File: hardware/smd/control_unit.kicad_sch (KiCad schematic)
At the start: 29 parts, among them J3 UART, K1 SPDT, 5V 72R, 10A 250VAC, Q1 NPN, 40V, 500mA, SW1 SW_Push, SW2 SW_Push, U5 ESP32-H2, Y1 32MHz ±10ppm CL8pF

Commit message: Add capacitor specifications, change capacity around crystal
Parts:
- C19: renamed from C24; value 10p 10V -> 8p 10V C0G
- C20: renamed from C25; value 10p 10V -> 8p 10V C0G
- renumbered C19 to C21, C20 to C22, C21 to C23, C22 to C24, C23 to C25, D5 to D4, D4 to D5, R9 to R10, R6 to R5, R5 to R6, R10 to R7, R7 to R8, R8 to R9, SW2 to SW1, SW1 to SW2

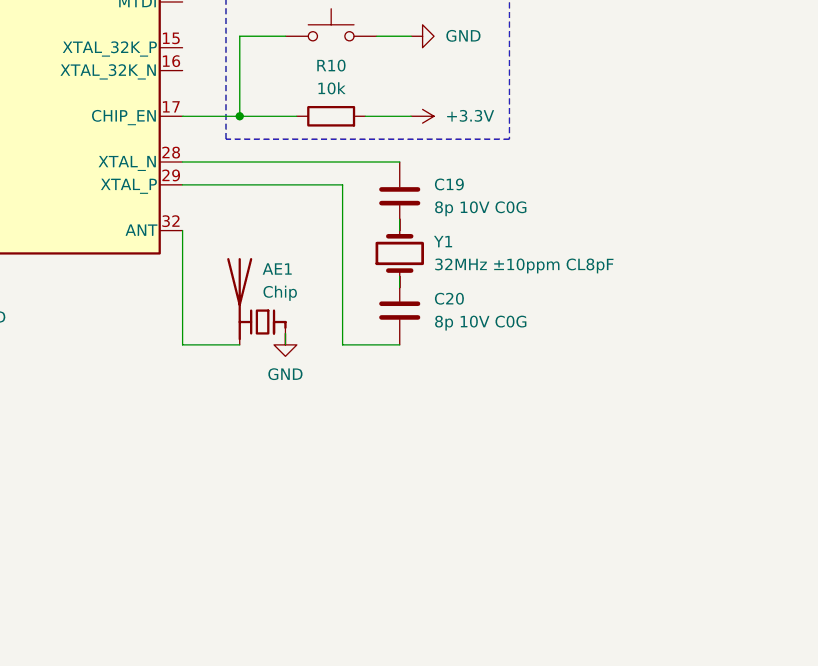
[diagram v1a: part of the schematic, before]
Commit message: Properly layout GND-fed antenna
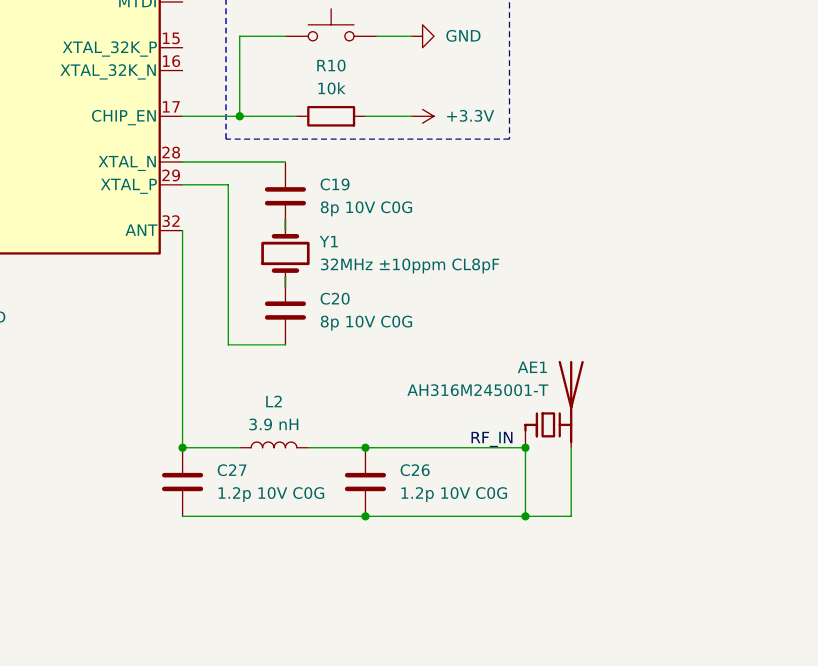
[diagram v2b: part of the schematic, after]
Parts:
- added C26, C27: 1.2p 10V C0G, symbol Device:C
- added L2: 3.9 nH, symbol Device:L
- AE1: value Chip -> AH316M245001-T
- D4: footprint Diode_THT:D_DO-41_SOD81_P10.16mm_Horizontal -> (none)
- D5, D6: footprint LED_THT:LED_D3.0mm -> (none)
- K1: footprint KiCadX_Relays_THT:Relay_SPDT_Relpol-RM51 -> (none)
- Q1: footprint Package_TO_SOT_THT:TO-92_Inline_Wide -> (none)
- R10, R5, R6, R7, R8, R9: footprint Resistor_THT:R_Axial_DIN0207_L6.3mm_D2.5mm_P7.62mm_Horizontal -> (none)
- U5: footprint KiCadX_MCU_Espressif:TQFN_32_1EP_4x4mm_P0.4mm_EP2.6x2.6mm_Standard -> (none)
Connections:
- net GND: no longer AE1.1 (FEED)
- net at U5.32 (ANT): now also C27.2, L2.1; no longer AE1.2 (PCB_Trace)
- new net RF_IN: AE1.1 (FEED), AE1.2 (PCB_Trace), C26.1, C26.2, C27.1, L2.2
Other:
- moved on the sheet: AE1, C19, C20, Y1

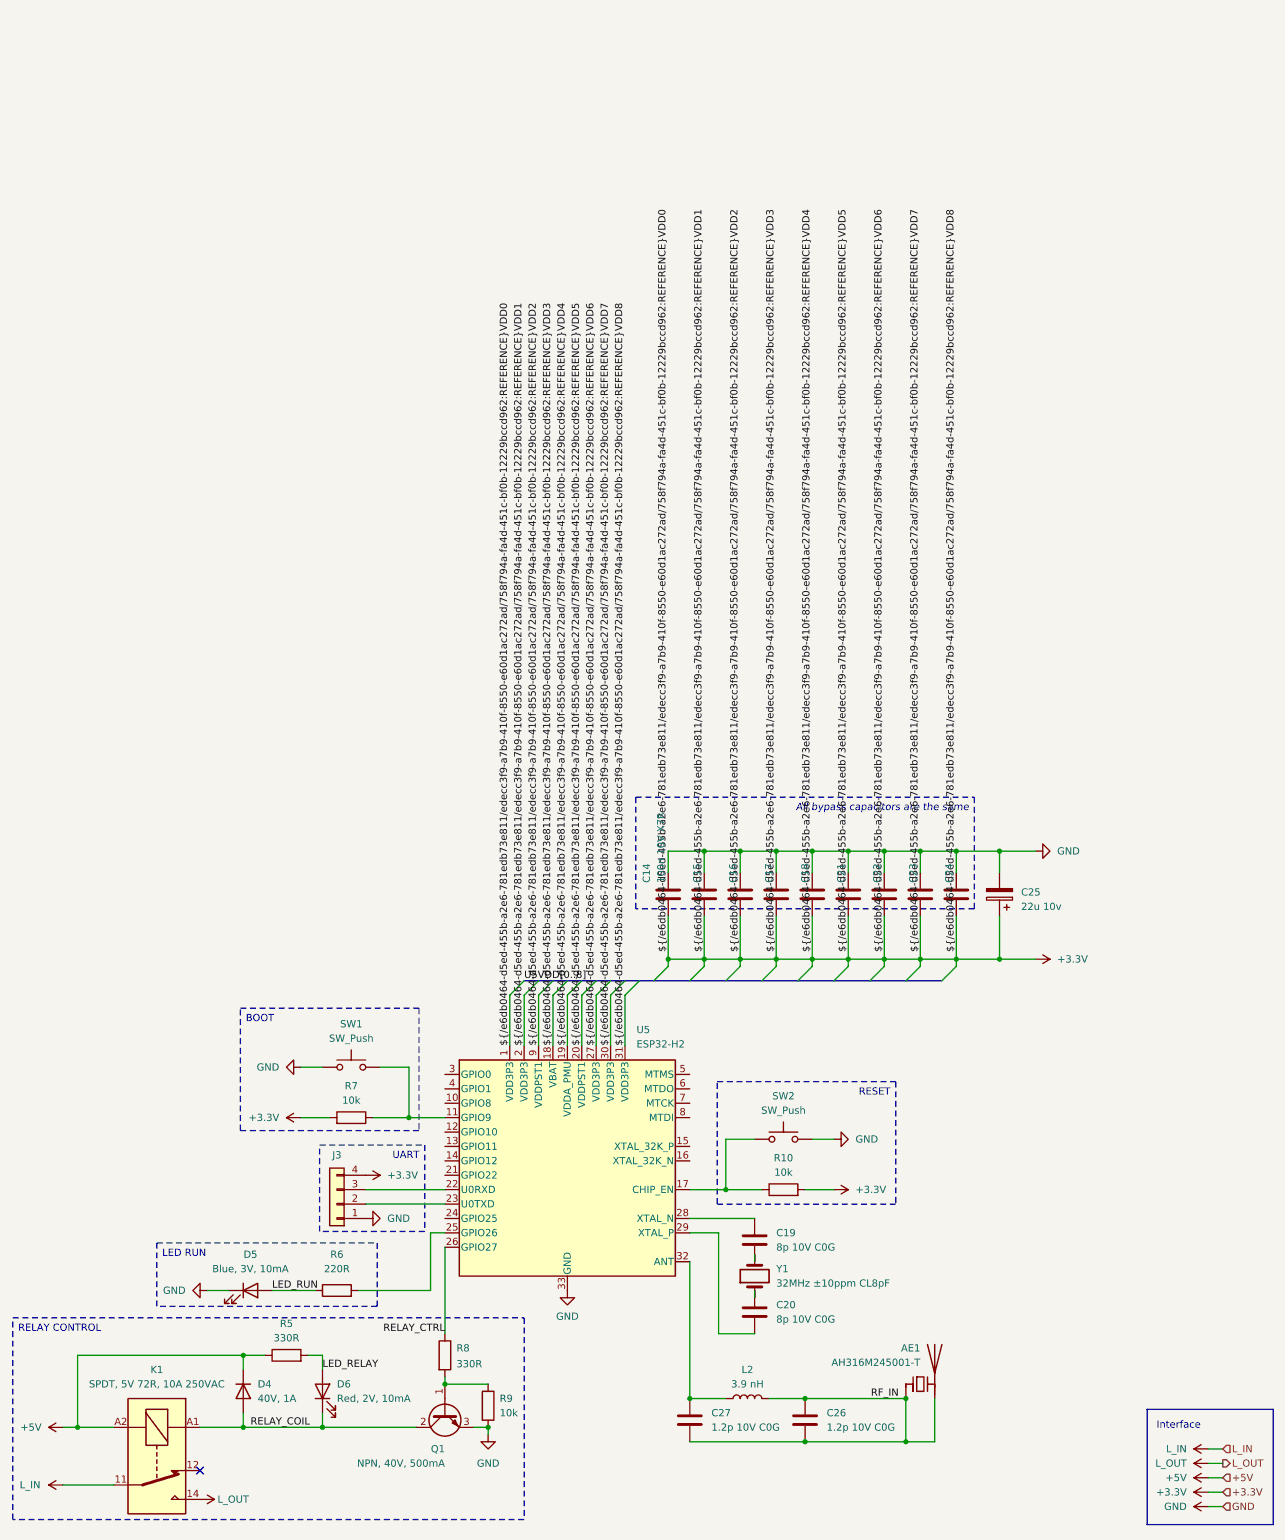
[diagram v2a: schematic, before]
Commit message: Assign footprints and JLC numbers (plus minor changes)
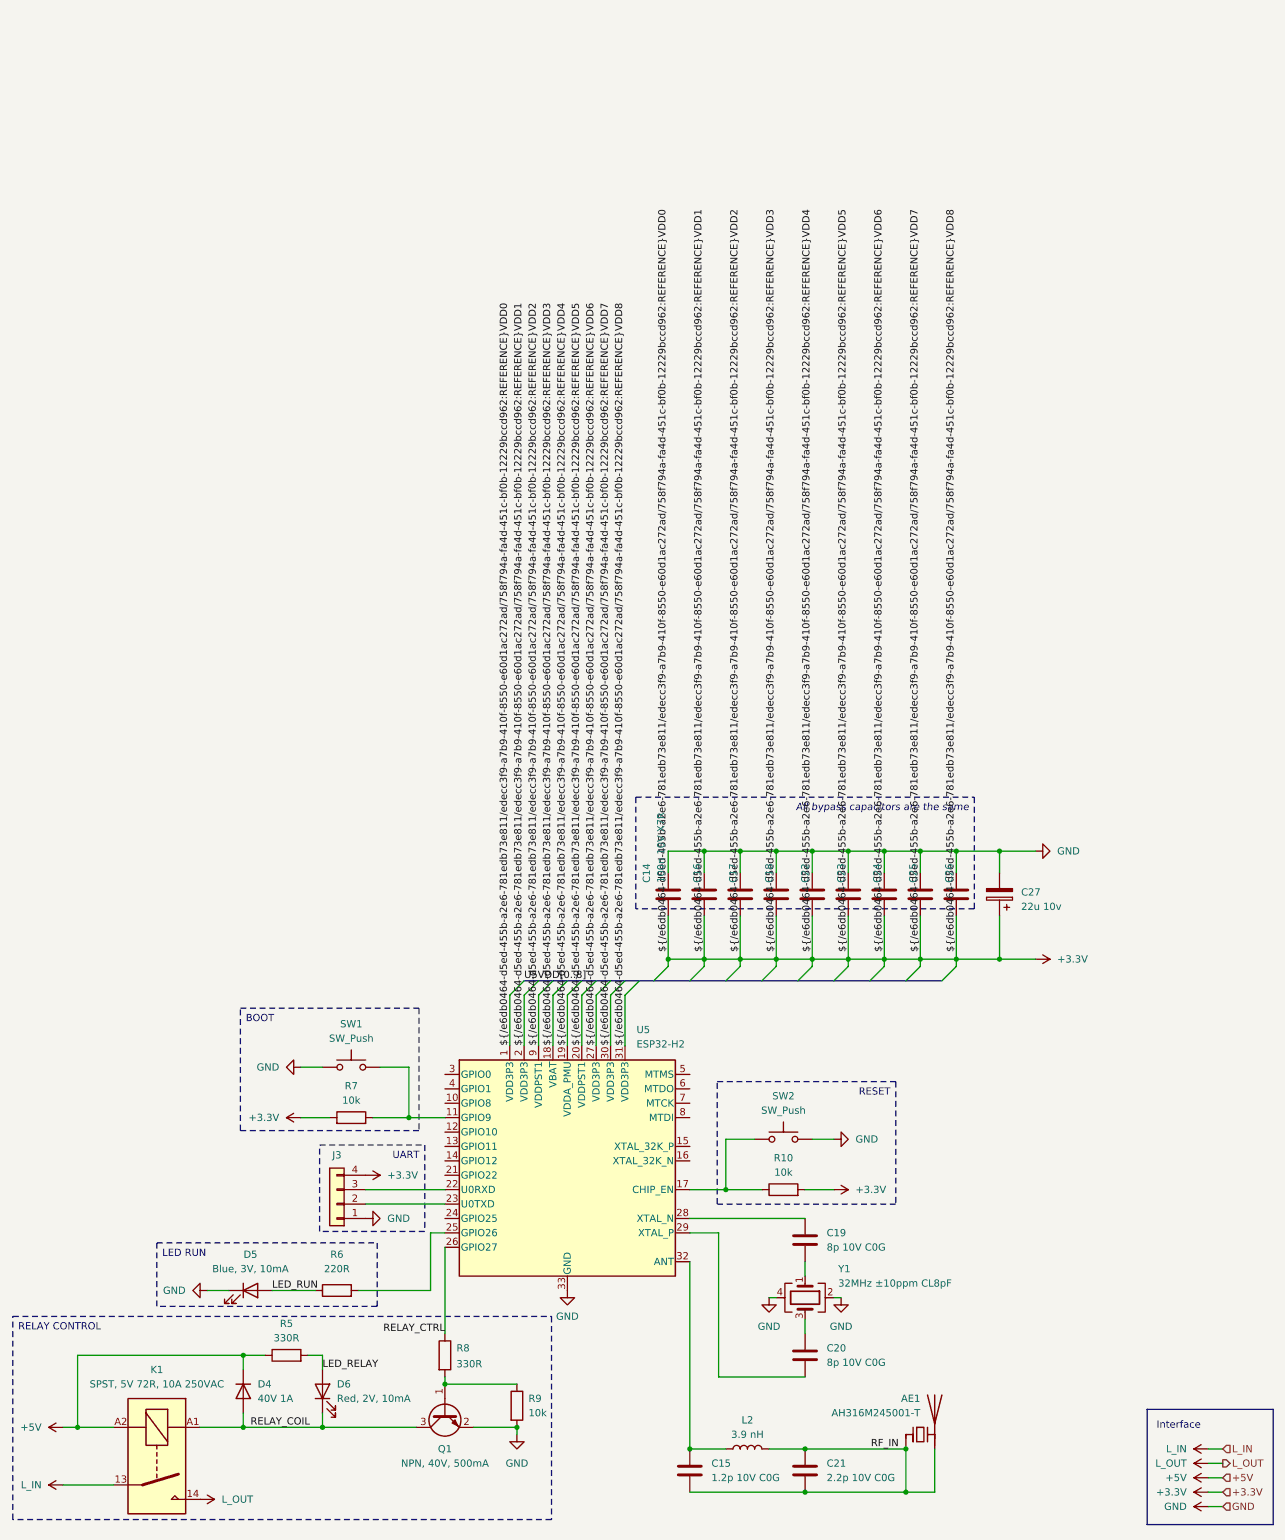
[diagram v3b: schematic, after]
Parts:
- removed K1: SPDT, 5V 72R, 10A 250VAC, symbol Relay:Relay_SPDT
- removed Q1: NPN, 40V, 500mA, symbol Transistor_BJT:Q_NPN_BCE
- removed Y1: 32MHz ±10ppm CL8pF, symbol Device:Crystal
- added K1: SPST, 5V 72R, 10A 250VAC, KiCadX_Relays_THT:Relay_SPST_OJ_SH_105HM_000, symbol Relay:Relay_SPST-NO
- added Q1: NPN, 40V, 500mA, Package_TO_SOT_SMD:SOT-323_SC-70, symbol Transistor_BJT:Q_NPN_BEC
- added Y1: 32MHz ±10ppm CL8pF, Crystal:Crystal_SMD_2016-4Pin_2.0x1.6mm, symbol Device:Crystal_GND24
- AE1: footprint (none) -> KiCadX_Antennas_SMD:AH316M245001_T; JLCPCB (none) -> C3285031
- C14: footprint (none) -> Capacitor_SMD:C_0402_1005Metric; JLCPCB (none) -> C309458
- C15: renamed from C27; footprint (none) -> Capacitor_SMD:C_0201_0603Metric; JLCPCB (none) -> C285021
- C16: renamed from C15; footprint (none) -> Capacitor_SMD:C_0402_1005Metric; JLCPCB (none) -> C309458
- C17: renamed from C16; footprint (none) -> Capacitor_SMD:C_0402_1005Metric; JLCPCB (none) -> C309458
- C18: renamed from C17; footprint (none) -> Capacitor_SMD:C_0402_1005Metric; JLCPCB (none) -> C309458
- C19, C20: footprint (none) -> Capacitor_SMD:C_0201_0603Metric; JLCPCB (none) -> C237455
- C21: renamed from C26; value 1.2p 10V C0G -> 2.2p 10V C0G; footprint (none) -> Capacitor_SMD:C_0201_0603Metric; JLCPCB (none) -> C710732
- C22: renamed from C18; footprint (none) -> Capacitor_SMD:C_0402_1005Metric; JLCPCB (none) -> C309458
- C23: renamed from C21; footprint (none) -> Capacitor_SMD:C_0402_1005Metric; JLCPCB (none) -> C309458
- C24: renamed from C22; footprint (none) -> Capacitor_SMD:C_0402_1005Metric; JLCPCB (none) -> C309458
- C25: renamed from C23; footprint (none) -> Capacitor_SMD:C_0402_1005Metric; JLCPCB (none) -> C309458
- C26: renamed from C24; footprint (none) -> Capacitor_SMD:C_0402_1005Metric; JLCPCB (none) -> C309458
- C27: renamed from C25; footprint (none) -> Capacitor_SMD:CP_Elec_5x5.4; JLCPCB (none) -> C22387966
- D4: value 40V, 1A -> 40V 1A; footprint (none) -> Diode_SMD:D_SOD-323; JLCPCB (none) -> C191023
- D5: footprint (none) -> LED_SMD:LED_0603_1608Metric; JLCPCB (none) -> C2288
- D6: footprint (none) -> LED_SMD:LED_0603_1608Metric; JLCPCB (none) -> C2286
- J3: footprint (none) -> Connector_PinHeader_2.54mm:PinHeader_1x04_P2.54mm_Vertical; JLCPCB (none) -> C2691448
- L2: footprint (none) -> Inductor_SMD:L_0402_1005Metric; JLCPCB (none) -> C77109
- R10, R7, R9: footprint (none) -> Resistor_SMD:R_0402_1005Metric; JLCPCB (none) -> C25744
- R5, R8: footprint (none) -> Resistor_SMD:R_0402_1005Metric; JLCPCB (none) -> C105875
- R6: footprint (none) -> Resistor_SMD:R_0402_1005Metric; JLCPCB (none) -> C25091
- SW1, SW2: footprint (none) -> Button_Switch_SMD:SW_SPST_TL3305A; JLCPCB (none) -> C18078070
- U5: footprint (none) -> KiCadX_MCU_Espressif:TQFN_32_1EP_4x4mm_P0.4mm_EP2.4x2.4mm_Compact; JLCPCB (none) -> C22470214
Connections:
- net +5V: now also K1.A2
- net GND: now also Q1.2 (E), Y1.2, Y1.4
- net L_IN: now also K1.13
- net L_OUT: now also K1.14
- net RELAY_COIL: now also K1.A1, Q1.3 (C)
- net at C20.1: now also Y1.3
- net at R8.2, R9.1: now also Q1.1 (B)
- net at C19.2: now also Y1.1
- no-connect marks 1 -> 0
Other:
- moved on the sheet: AE1, C15, C19, C20, C21, L2, R9

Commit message: Complete PCB and schematics after fucking a lot of iterations
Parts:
- removed C16, C22, C23, C26: 100n 10V X7R, Capacitor_SMD:C_0402_1005Metric, symbol Device:C
- removed C27: 22u 10v, Capacitor_SMD:CP_Elec_5x5.4, symbol Device:C_Polarized
- removed J3: UART, Connector_PinHeader_2.54mm:PinHeader_1x04_P2.54mm_Vertical, symbol Connector_Generic:Conn_01x04
- removed SW1, SW2: SW_Push, Button_Switch_SMD:SW_SPST_TL3305A, symbol Switch:SW_Push
- added J5: UART, Connector_PinHeader_1.27mm:PinHeader_1x04_P1.27mm_Vertical, symbol Connector:Conn_01x04_Pin
- added J6: Conn_01x02_Pin, Connector_PinHeader_1.27mm:PinHeader_1x02_P1.27mm_Vertical, symbol Connector:Conn_01x02_Pin
- AE1: value AH316M245001-T -> Antenna_Chip; footprint KiCadX_Antennas_SMD:AH316M245001_T -> KiCadX_Antennas_SMD:PCB_antenna_Espressif_2.4GHz_right; JLCPCB C3285031 -> (none); now left out of the parts list
- C15: value 1.2p 10V C0G -> 5.6p C0G; JLCPCB C285021 -> C85914
- C18: renamed from C21; value 2.2p 10V C0G -> 2.2p C0G
- K1: JLCPCB OJ-SH-105HM,000 -> C1564132
- renumbered C17 to C16, C20 to C17, C18 to C19, C24 to C20, C19 to C21, C25 to C22, L2 to L1
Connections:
- net +3.3V: now also J5.1 (Pin_1)
- net +5V: now also K1.A1; no longer K1.A2
- net GND: now also AE1.2 (PCB_Trace), C17.2, C18.1, C21.1, L1.2, J5.4 (Pin_4)
- net LED_RUN: now also R6.2, U5.25 (GPIO26); no longer D5.2 (A), R6.1
- net L_IN: now also K1.14; no longer K1.13
- net L_OUT: now also K1.13; no longer K1.14
- net RELAY_COIL: now also K1.A2; no longer K1.A1
- net at C17.1: now also U5.29 (XTAL_P), Y1.1; no longer Y1.3
- net RESET: now reaches R10.1, U5.17 (CHIP_EN)
- net RESET: now also J6.2 (Pin_2)
- net BOOT: now reaches R7.1, U5.11 (GPIO9)
- net BOOT: now also J6.1 (Pin_1)
- net at C21.2: now also U5.28 (XTAL_N), Y1.3; no longer Y1.1
- net TX: now reaches U5.22 (U0RXD)
- net TX: now also J5.2 (Pin_2)
- net RX: now reaches U5.23 (U0TXD)
- net RX: now also J5.3 (Pin_3)
- net RF: now reaches C15.2, L1.1, U5.32 (ANT)
- net RF_IN: no longer names the net of AE1.1 (FEED), C15.1, C18.2
- net RF_IN: no longer AE1.2 (PCB_Trace), C18.1, L1.2
- new net: D5.2 (A), R6.1
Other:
- moved on the sheet: C14, C15, C16, C17, C18, C19, C20, C21, C22, K1, L1, R6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

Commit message: Rename JLCPCB property to LCSC PN across schematic files
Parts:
- C14, C16, C19, C20, C22: JLCPCB C309458 -> (none); LCSC PN (none) -> C309458
- C15: JLCPCB C85914 -> (none); LCSC PN (none) -> C85914
- C17, C21: JLCPCB C237455 -> (none); LCSC PN (none) -> C237455
- C18: JLCPCB C710732 -> (none); LCSC PN (none) -> C710732
- D4: JLCPCB C191023 -> (none); LCSC PN (none) -> C191023
- D5: JLCPCB C2288 -> (none); LCSC PN (none) -> C2288
- D6: JLCPCB C2286 -> (none); LCSC PN (none) -> C2286
- J5: JLCPCB C41366759 -> (none); LCSC PN (none) -> C41366759
- J6: JLCPCB C7470078 -> (none); LCSC PN (none) -> C7470078
- K1: JLCPCB C1564132 -> (none); LCSC PN (none) -> C1564132
- L1: JLCPCB C77109 -> (none); LCSC PN (none) -> C77109
- Q1: JLCPCB C383232 -> (none); LCSC PN (none) -> C383232
- R10, R7, R9: JLCPCB C25744 -> (none); LCSC PN (none) -> C25744
- R5, R8: JLCPCB C105875 -> (none); LCSC PN (none) -> C105875
- R6: JLCPCB C25091 -> (none); LCSC PN (none) -> C25091
- U5: JLCPCB C22470214 -> (none); LCSC PN (none) -> C22470214
- Y1: JLCPCB C2965582 -> (none); LCSC PN (none) -> C2965582
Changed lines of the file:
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@@
 			)
 		)
-		(property "JLCPCB" "C309458"
-			(at 172.72 46.99 0)
+		(property "LCSC PN" "C309458"
+			(at 172.72 46.99 90)
 			(effects
 				(font
@@
 			)
 		)
-		(property "JLCPCB" "C237455"
+		(property "LCSC PN" "C237455"
 			(at 185.42 118.11 0)
 			(effects
@@
 			)
 		)
-		(property "JLCPCB" "C309458"
-			(at 210.82 46.99 0)
+		(property "LCSC PN" "C309458"
+			(at 210.82 46.99 90)
 			(effects
 				(font
@@
 			)
 		)
-		(property "JLCPCB" "C25744"
-			(at 193.04 101.6 0)
+		(property "LCSC PN" "C25744"
+			(at 193.04 101.6 90)
 			(effects
 				(font
@@
 			)
 		)
-		(property "JLCPCB" "C2286"
-			(at 111.76 137.16 0)
+		(property "LCSC PN" "C2286"
+			(at 111.76 137.16 90)
 			(effects
 				(font
@@
 			)
 		)
-		(property "JLCPCB" "C710732"
+		(property "LCSC PN" "C710732"
 			(at 189.23 149.86 0)
 			(effects
@@
 			)
 		)
-		(property "JLCPCB" "C41366759"
+		(property "LCSC PN" "C41366759"
 			(at 111.76 101.6 0)
 			(effects
@@
 			)
 		)
-		(property "JLCPCB" "C105875"
-			(at 105.41 130.81 0)
+		(property "LCSC PN" "C105875"
+			(at 105.41 130.81 90)
 			(effects
 				(font
@@
 			)
 		)
-		(property "JLCPCB" "C191023"
-			(at 97.79 137.16 0)
+		(property "LCSC PN" "C191023"
+			(at 97.79 137.16 90)
 			(effects
 				(font
@@
 			)
 		)
-		(property "JLCPCB" "C25091"
-			(at 111.76 119.38 0)
+		(property "LCSC PN" "C25091"
+			(at 111.76 119.38 90)
 			(effects
 				(font
@@
 			)
 		)
-		(property "JLCPCB" "C383232"
-			(at 133.35 140.97 0)
+		(property "LCSC PN" "C383232"
+			(at 133.35 140.97 90)
 			(effects
 				(font
@@
 			)
 		)
-		(property "JLCPCB" "C2965582"
+		(property "LCSC PN" "C2965582"
 			(at 204.47 121.92 0)
 			(effects
@@
 			)
 		)
-		(property "JLCPCB" "C2288"
+		(property "LCSC PN" "C2288"
 			(at 99.06 119.38 0)
 			(effects
@@
 			)
 		)
-		(property "JLCPCB" "C22470214"
+		(property "LCSC PN" "C22470214"
 			(at 154.94 97.79 0)
 			(effects
@@
 			)
 		)
-		(property "JLCPCB" "C85914"
-			(at 182.88 144.78 0)
+		(property "LCSC PN" "C85914"
+			(at 182.88 144.78 90)
 			(effects
 				(font
@@
 			)
 		)
-		(property "JLCPCB" "C309458"
-			(at 191.77 46.99 0)
+		(property "LCSC PN" "C309458"
+			(at 191.77 46.99 90)
 			(effects
 				(font
@@
 			)
 		)
-		(property "JLCPCB" "C7470078"
+		(property "LCSC PN" "C7470078"
 			(at 111.76 64.77 0)
 			(effects
@@
 			)
 		)
-		(property "JLCPCB" "C237455"
+		(property "LCSC PN" "C237455"
 			(at 212.09 125.73 0)
 			(effects
@@
 			)
 		)
-		(property "JLCPCB" "C25744"
+		(property "LCSC PN" "C25744"
 			(at 146.05 139.7 0)
 			(effects
@@
 			)
 		)
-		(property "JLCPCB" "C309458"
-			(at 185.42 46.99 0)
+		(property "LCSC PN" "C309458"
+			(at 185.42 46.99 90)
 			(effects
 				(font
@@
 			)
 		)
-		(property "JLCPCB" "C25744"
-			(at 116.84 88.9 0)
+		(property "LCSC PN" "C25744"
+			(at 116.84 88.9 90)
 			(effects
 				(font
@@
 			)
 		)
-		(property "JLCPCB" "C105875"
+		(property "LCSC PN" "C105875"
 			(at 133.35 130.81 0)
 			(effects
@@
 			)
 		)
-		(property "JLCPCB" "C1564132"
-			(at 82.55 148.59 0)
+		(property "LCSC PN" "C1564132"
+			(at 82.55 148.59 90)
 			(effects
 				(font
@@
 			)
 		)
-		(property "JLCPCB" "C77109"
+		(property "LCSC PN" "C77109"
 			(at 176.53 149.86 0)
 			(effects
@@
 			)
 		)
-		(property "JLCPCB" "C309458"
-			(at 217.17 46.99 0)
+		(property "LCSC PN" "C309458"
+			(at 217.17 46.99 90)
 			(effects
 				(font

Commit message: Update library paths from KiCadX to PCM_SKC
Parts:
- U5: symbol KiCadX_MCU_Espressif:ESP32-H2 -> PCM_SKC_MCU_Espressif:ESP32-H2
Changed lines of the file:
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@@
 	)
 	(symbol
-		(lib_id "KiCadX_MCU_Espressif:ESP32-H2")
+		(lib_id "PCM_SKC_MCU_Espressif:ESP32-H2")
 		(at 154.94 97.79 0)
 		(unit 1)
